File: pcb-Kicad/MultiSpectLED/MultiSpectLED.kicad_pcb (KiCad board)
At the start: 2 copper layers, 113.4 x 56 mm, 117 parts, among them J1 Conn_01x02_Female, J2 USB_C_Receptacle_USB2.0, SW1 NKK_HEXADEC, SW2 NKK_HEXADEC, U1 PAM2804, U10 PAM2804, U11 PAM2804, U12 PAM2804, U13 PAM2804, U14 PAM2804, U15 PAM2804, U16 PAM2804, U2 TeensyLC, U3 PAM2804, U4 PAM2804, U5 PAM2804, U6 PAM2804, U7 PAM2804, U8 PAM2804, U9 PAM2804

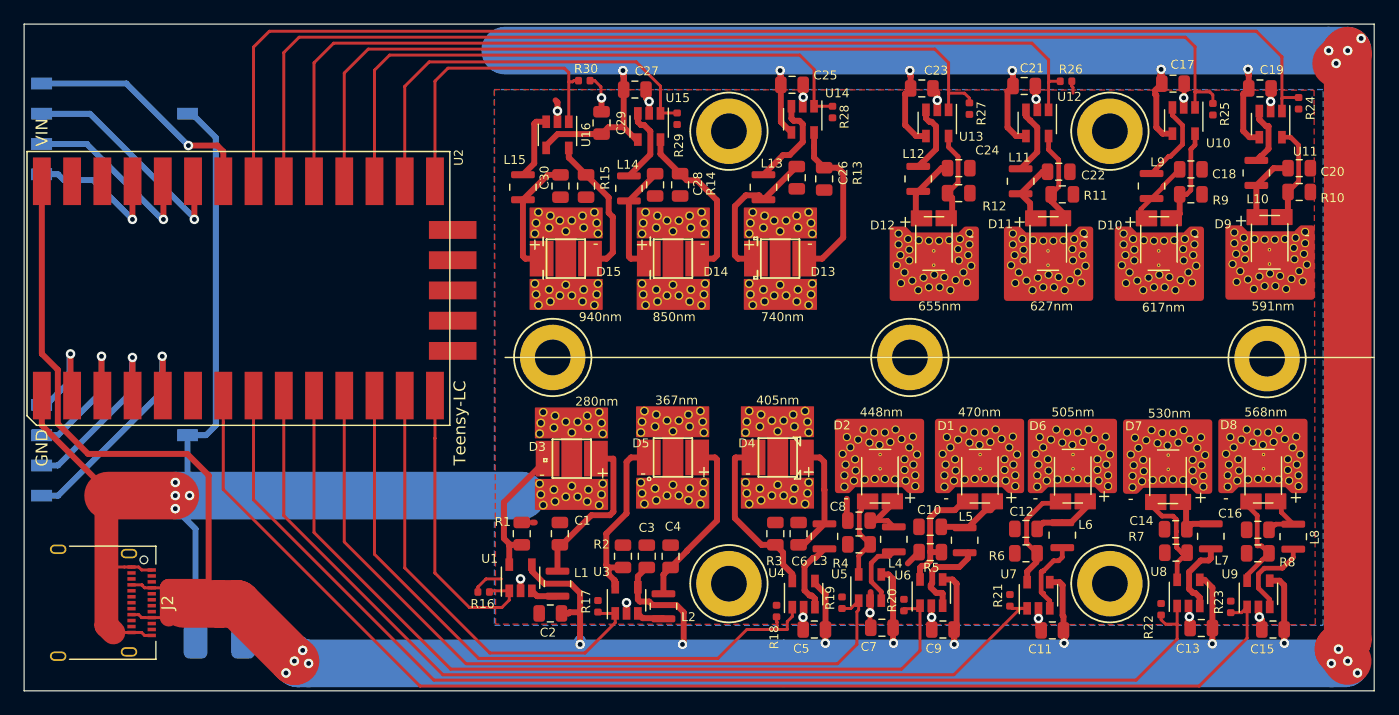
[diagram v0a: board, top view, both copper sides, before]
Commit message: Change the power input socket to a 2.1mm DC jack instead of the USB-C connector (which wasn't available)
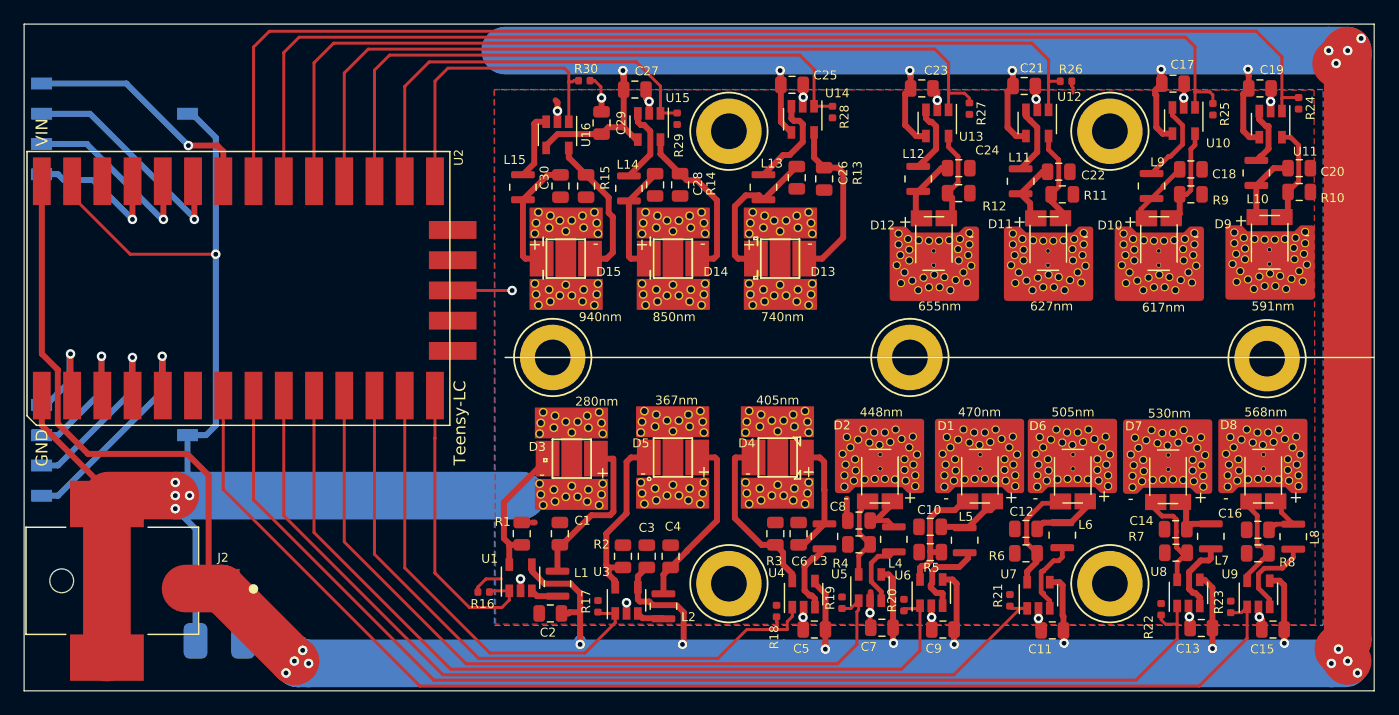
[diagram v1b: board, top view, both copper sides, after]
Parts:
- J2: value USB_C_Receptacle_USB2.0 -> PJ-036AH-SMT-TR; footprint MultiSpectLED:USB_C_Receptacle_Amphenol_12401610E4-2A -> MultiSpectLED:CUI_PJ-036AH-SMT-TR
- moved J2 10.3 mm to (139.5, 112.4), turned to 0 degrees
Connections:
- U2 pad 17_5V: Net-(U2-Pad17_5V) -> unconnected-(U2-Pad17_5V)
- U2 pad 26: Net-(U2-Pad26) -> unconnected-(U2-Pad26)
- U2 pad 33Va: Net-(U2-Pad33Va) -> unconnected-(U2-Pad33Va)
- U2 pad 33Vb: Net-(U2-Pad33Vb) -> unconnected-(U2-Pad33Vb)
- U2 pad 4: Net-(U2-Pad4) -> unconnected-(U2-Pad4)
- U2 pad GNDb: Net-(U2-PadGNDb) -> /GND
- U2 pad GNDc: Net-(U2-PadGNDc) -> /GND
- U2 pad PRG: Net-(U2-PadPRG) -> unconnected-(U2-PadPRG)
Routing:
- net /GND: track 148.0 -> 161.4 mm, vias 20 -> 22
- net /+5V: track 395.2 -> 383.2 mm
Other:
- net class Default removed
